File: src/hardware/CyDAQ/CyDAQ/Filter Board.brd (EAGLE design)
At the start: 160 x 110 mm, 215 parts, among them J1 DCJ0202, J10 Vout_HEADER, J11 5V0_SENSOR, J12 3V3_SENSOR, J13 1V8_SENSOR, J14 BRKOUT_JD, J15 BRKOUT_JC, J16 BRKOUT_JB, J17 BRKOUT_JF, J18 5V0_CONN, J19 3V3_CONN, J2 ZYBO_JF, J20 1V8_CONN, J21 BRKOUT_JD, J22 ZYBO_Power, J23 ZYBO_Power, J3 ZYBO_JE, J4 ZYBO_JD, J5 ZYBO_JC, J6 ZYBO_JB, J7 A_XADC, J8 SJ1-3523N, J9 Vin_HEADER, U1 TPS54531DDARDDA8_3P1X2P4-L, U10 CD74HCT4051, U11 CD74HCT4051, U12 OPA4197, U13 OPA4197, U14 OPA4197, U15 OPA4197, U16 OPA4197, U17 CD74HCT4053, U18 CD74HCT4051, U19 OPA2197, U3 TPS56339, U4 TPS56339, U5 LM43601PWPR, U6 X9258, U7 X9258, U8 X9258, U9 X9258

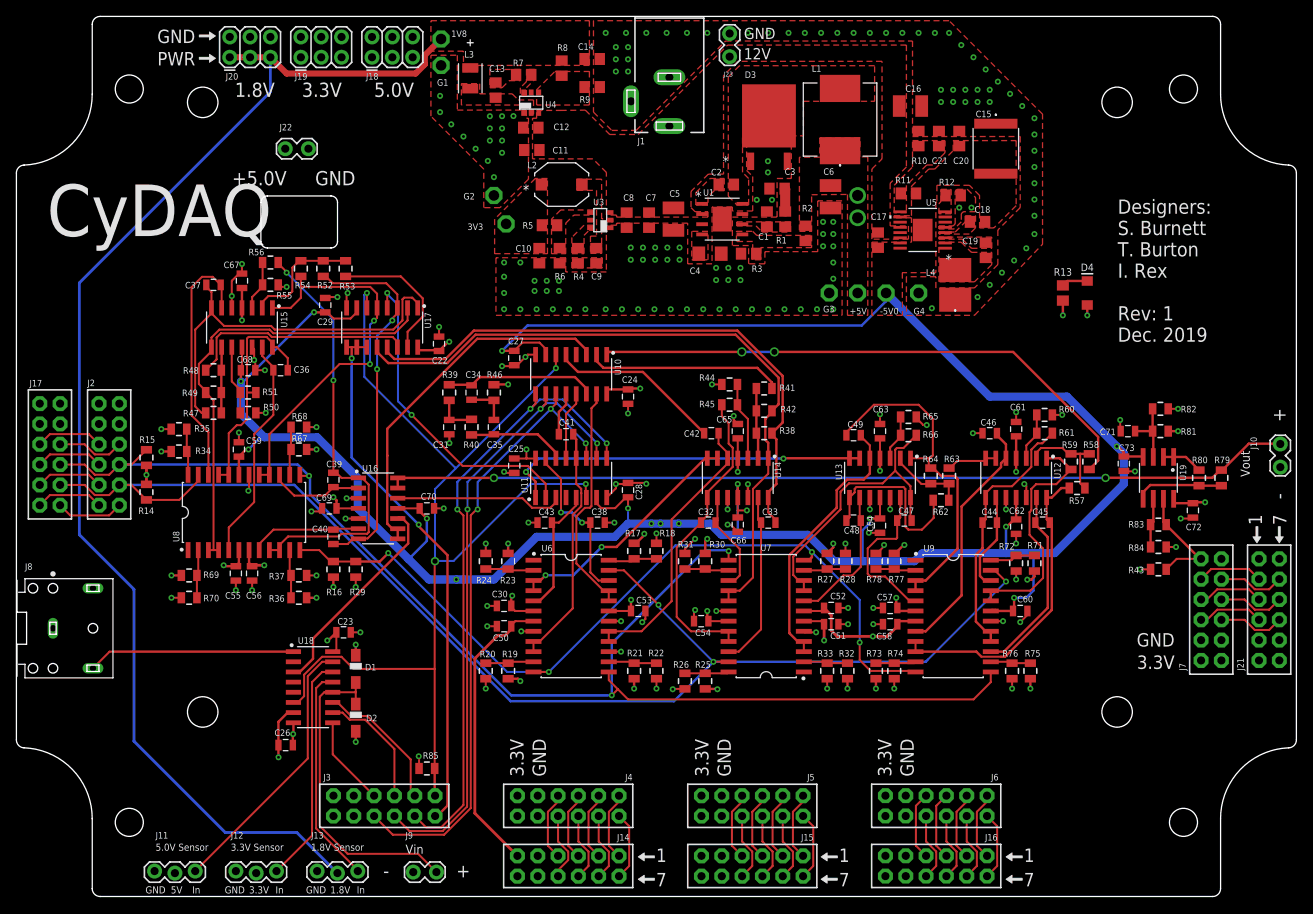
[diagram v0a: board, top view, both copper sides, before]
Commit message: Changed silkscreen and minor mechancial changes
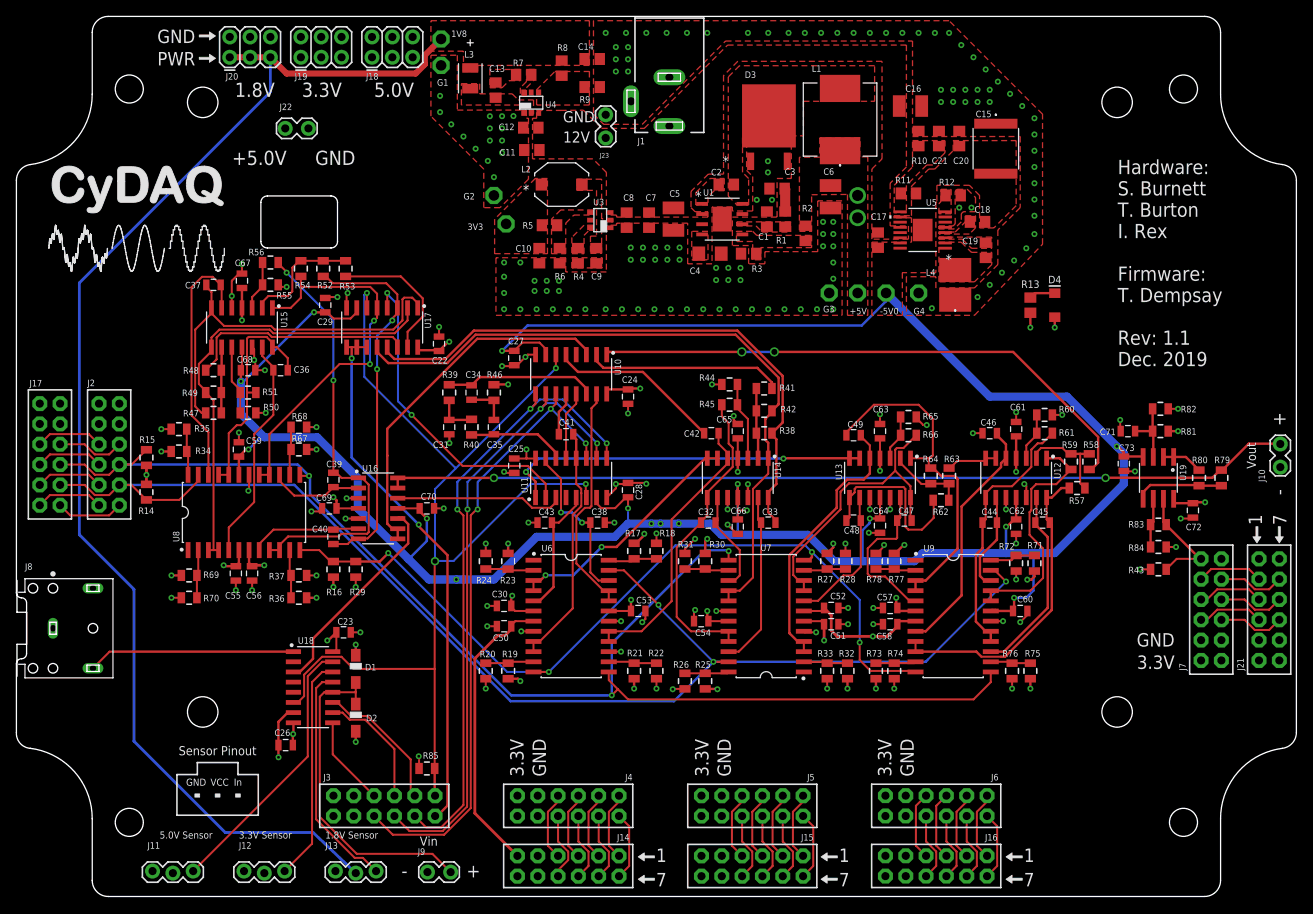
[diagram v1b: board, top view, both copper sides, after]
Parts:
- moved J23 18.5 mm to (73.7, 97.5)
- moved R13 4.34 mm to (126.7, 73.9)
- moved D4 4.34 mm to (129.8, 73.9)
- moved J22 2.54 mm to (36.3, 96.0)
- moved J13 2.29 mm to (39.9, 3.05)
- moved J9 1.78 mm to (51.6, 3.05)
- moved J12 1.02 mm to (28.4, 3.05)
- moved C66 0.25 mm to (90.2, 46.2)
- moved J11 0.25 mm to (17.0, 3.05)
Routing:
- net +1V8: track 160.2 -> 162.4 mm
- net 1V8SENSOR_IN: track 27.4 -> 28.9 mm
- net +3V3: track 434.6 -> 435.7 mm
- net ANALOGUE_IN: track 40.5 -> 41.7 mm
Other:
- outline, holes or cut-outs redrawn
- board text added: "+5V"
- board text added: "-5V"
- board text added: "1V8"
- board text added: "3V3"
- board text added: "5V0"
- board text added: "Hardware: S. Burnett T. Burton I. Rex Firmware: T. Dempsay Rev: 1.1 Dec. 2019"
- board text added: "Sensor Pinout"
- board text added: "VCC"
- board text removed: "5V"
- board text removed: "CyDAQ"
- board text removed: "Designers: S. Burnett T. Burton I. Rex Rev: 1 Dec. 2019"

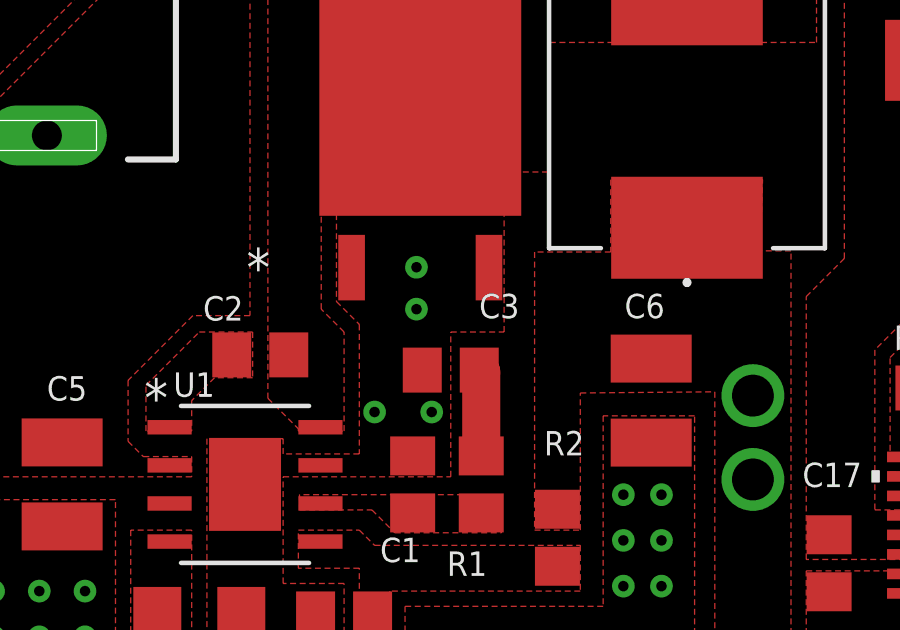
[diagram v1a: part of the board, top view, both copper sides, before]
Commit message: Adjusted C3 Silkscreen and added 3D renders
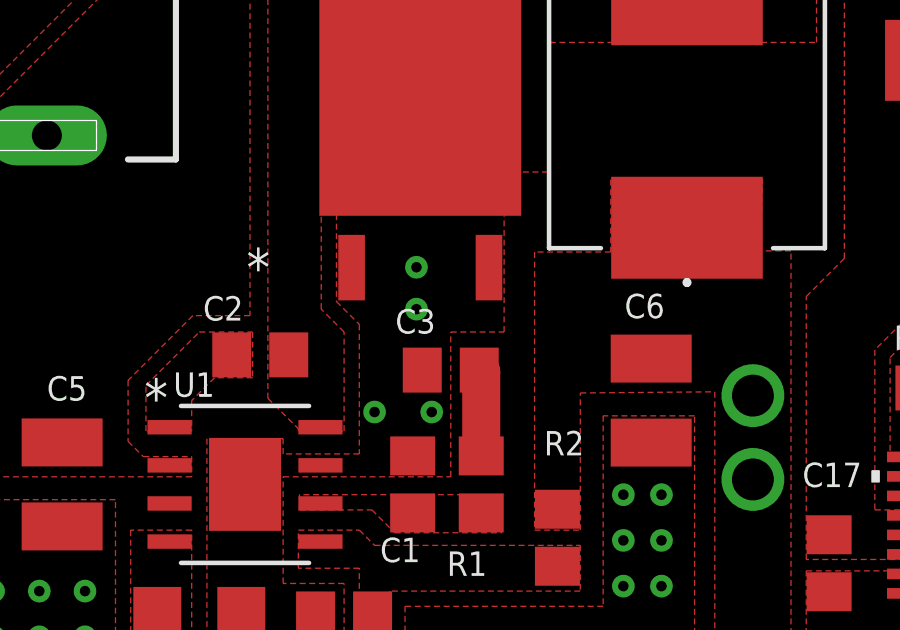
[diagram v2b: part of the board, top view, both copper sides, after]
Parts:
- J23: value ZYBO_Power -> INPUT_PWR
